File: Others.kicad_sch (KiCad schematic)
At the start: 9 parts, among them J16 UFL, Q14 SI2312BDS

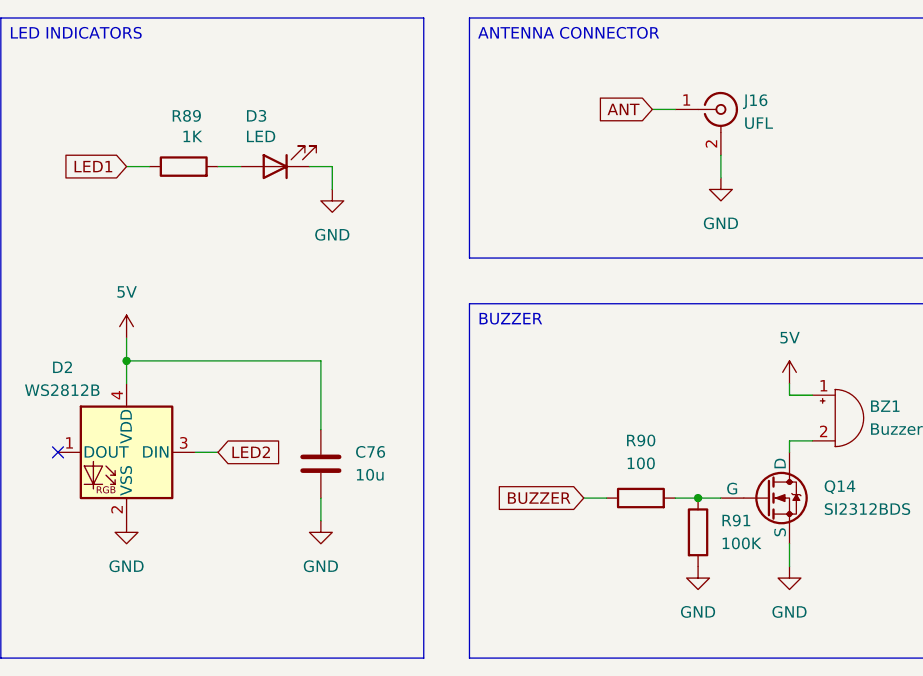
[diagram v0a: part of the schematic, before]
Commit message: Connectors and tag
Added bulk capacitance for each ESC.
Added SWD connector.
Updated all tags.

TODO:
Add pads for the unconnected GPIO pins.
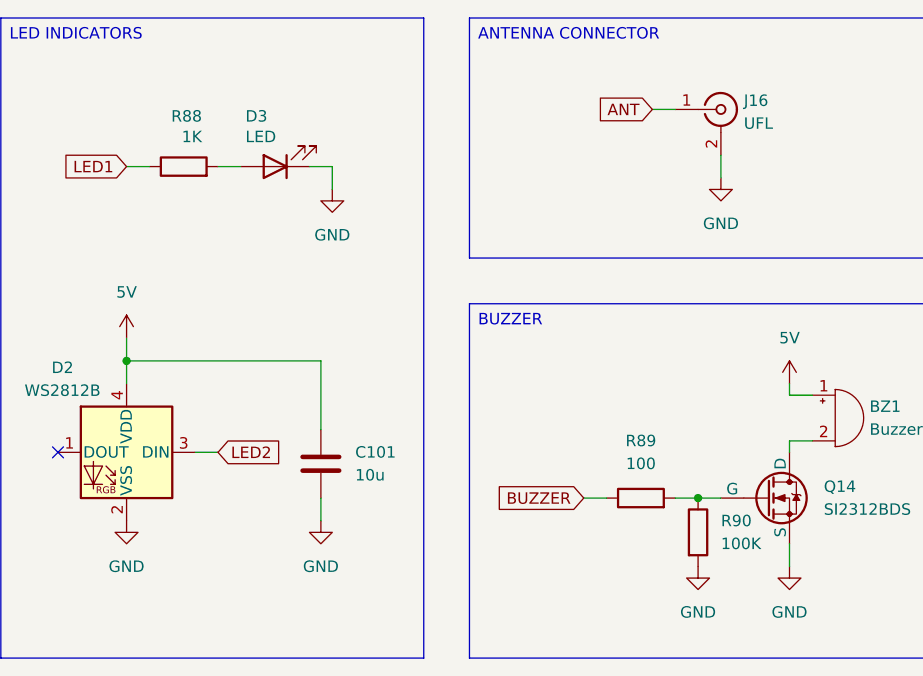
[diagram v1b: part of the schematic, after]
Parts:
- renumbered C76 to C101, R89 to R88, R90 to R89, R91 to R90
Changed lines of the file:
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@@
 		(on_board yes)
 		(dnp no)
-		(property "Reference" "#PWR0186"
+		(property "Reference" "#PWR0198"
 			(at 125.73 85.09 0)
 			(effects
@@
 			(project "ThunderHorse"
 				(path "/ac187c6c-fa53-41cc-bce1-6f39a42a92e8/111cf19a-e0f8-4ba5-b5cb-1102d2b05aed"
-					(reference "#PWR0186")
+					(reference "#PWR0198")
 					(unit 1)
 				)
@@
 		(dnp no)
 		(fields_autoplaced yes)
-		(property "Reference" "#PWR0187"
+		(property "Reference" "#PWR0199"
 			(at 166.37 127 0)
 			(effects
@@
 			(project "ThunderHorse"
 				(path "/ac187c6c-fa53-41cc-bce1-6f39a42a92e8/111cf19a-e0f8-4ba5-b5cb-1102d2b05aed"
-					(reference "#PWR0187")
+					(reference "#PWR0199")
 					(unit 1)
 				)
@@
 		(dnp no)
 		(fields_autoplaced yes)
-		(property "Reference" "#PWR0184"
+		(property "Reference" "#PWR0196"
 			(at 102.87 121.92 0)
 			(effects
@@
 			(project "ThunderHorse"
 				(path "/ac187c6c-fa53-41cc-bce1-6f39a42a92e8/111cf19a-e0f8-4ba5-b5cb-1102d2b05aed"
-					(reference "#PWR0184")
+					(reference "#PWR0196")
 					(unit 1)
 				)
@@
 		(dnp no)
 		(fields_autoplaced yes)
-		(property "Reference" "#PWR0185"
+		(property "Reference" "#PWR0197"
 			(at 124.46 121.92 0)
 			(effects
@@
 			(project "ThunderHorse"
 				(path "/ac187c6c-fa53-41cc-bce1-6f39a42a92e8/111cf19a-e0f8-4ba5-b5cb-1102d2b05aed"
-					(reference "#PWR0185")
+					(reference "#PWR0197")
 					(unit 1)
 				)
@@
 		(dnp no)
 		(fields_autoplaced yes)
-		(property "Reference" "#PWR0188"
+		(property "Reference" "#PWR0200"
 			(at 168.91 83.82 0)
 			(effects
@@
 			(project "ThunderHorse"
 				(path "/ac187c6c-fa53-41cc-bce1-6f39a42a92e8/111cf19a-e0f8-4ba5-b5cb-1102d2b05aed"
-					(reference "#PWR0188")
+					(reference "#PWR0200")
 					(unit 1)
 				)
@@
 		(on_board yes)
 		(dnp no)
-		(property "Reference" "#PWR0189"
+		(property "Reference" "#PWR0201"
 			(at 176.53 104.14 0)
 			(effects
@@
 			(project "ThunderHorse"
 				(path "/ac187c6c-fa53-41cc-bce1-6f39a42a92e8/111cf19a-e0f8-4ba5-b5cb-1102d2b05aed"
-					(reference "#PWR0189")
+					(reference "#PWR0201")
 					(unit 1)
 				)
@@
 		(dnp no)
 		(fields_autoplaced yes)
-		(property "Reference" "R90"
+		(property "Reference" "R89"
 			(at 160.02 106.68 90)
 			(effects
@@
 			(project "ThunderHorse"
 				(path "/ac187c6c-fa53-41cc-bce1-6f39a42a92e8/111cf19a-e0f8-4ba5-b5cb-1102d2b05aed"
-					(reference "R90")
+					(reference "R89")
 					(unit 1)
 				)
@@
 		(on_board yes)
 		(dnp no)
-		(property "Reference" "R89"
+		(property "Reference" "R88"
 			(at 111.252 70.612 90)
 			(effects
@@
 			(project "ThunderHorse"
 				(path "/ac187c6c-fa53-41cc-bce1-6f39a42a92e8/111cf19a-e0f8-4ba5-b5cb-1102d2b05aed"
-					(reference "R89")
+					(reference "R88")
 					(unit 1)
 				)
@@
 		(dnp no)
 		(fields_autoplaced yes)
-		(property "Reference" "R91"
+		(property "Reference" "R90"
 			(at 168.91 115.5699 0)
 			(effects
@@
 			(project "ThunderHorse"
 				(path "/ac187c6c-fa53-41cc-bce1-6f39a42a92e8/111cf19a-e0f8-4ba5-b5cb-1102d2b05aed"
-					(reference "R91")
+					(reference "R90")
 					(unit 1)
 				)
@@
 		(dnp no)
 		(fields_autoplaced yes)
-		(property "Reference" "C76"
+		(property "Reference" "C101"
 			(at 128.27 107.9499 0)
 			(effects
@@
 			(project "ThunderHorse"
 				(path "/ac187c6c-fa53-41cc-bce1-6f39a42a92e8/111cf19a-e0f8-4ba5-b5cb-1102d2b05aed"
-					(reference "C76")
+					(reference "C101")
 					(unit 1)
 				)
@@
 		(dnp no)
 		(fields_autoplaced yes)
-		(property "Reference" "#PWR0190"
+		(property "Reference" "#PWR0202"
 			(at 176.53 127 0)
 			(effects
@@
 			(project "ThunderHorse"
 				(path "/ac187c6c-fa53-41cc-bce1-6f39a42a92e8/111cf19a-e0f8-4ba5-b5cb-1102d2b05aed"
-					(reference "#PWR0190")
+					(reference "#PWR0202")
 					(unit 1)
 				)
@@
 		(on_board yes)
 		(dnp no)
-		(property "Reference" "#PWR0183"
+		(property "Reference" "#PWR0195"
 			(at 102.87 99.06 0)
 			(effects
@@
 			(project "ThunderHorse"
 				(path "/ac187c6c-fa53-41cc-bce1-6f39a42a92e8/111cf19a-e0f8-4ba5-b5cb-1102d2b05aed"
-					(reference "#PWR0183")
-					(unit 1)
-				)
+					(reference "#PWR0195")
+					(unit 1)
+				)

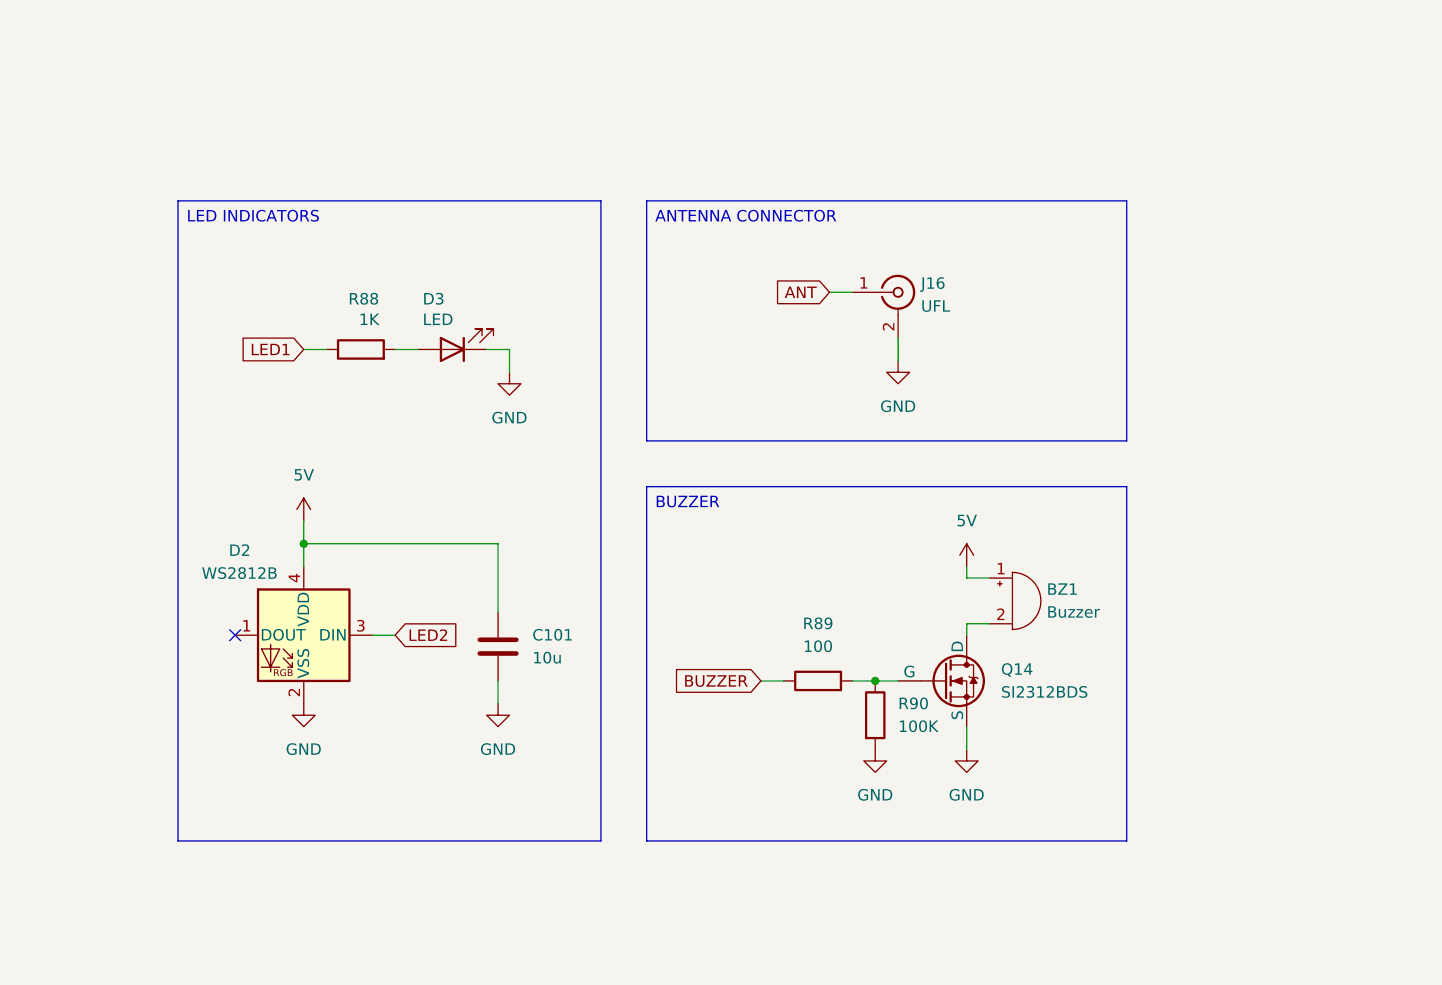
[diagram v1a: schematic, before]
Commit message: Missing labels and revision
First complete revision of the schematic.
Added missing labels.

TODO:
Continue reviewing the schematic.
Include net coloring.
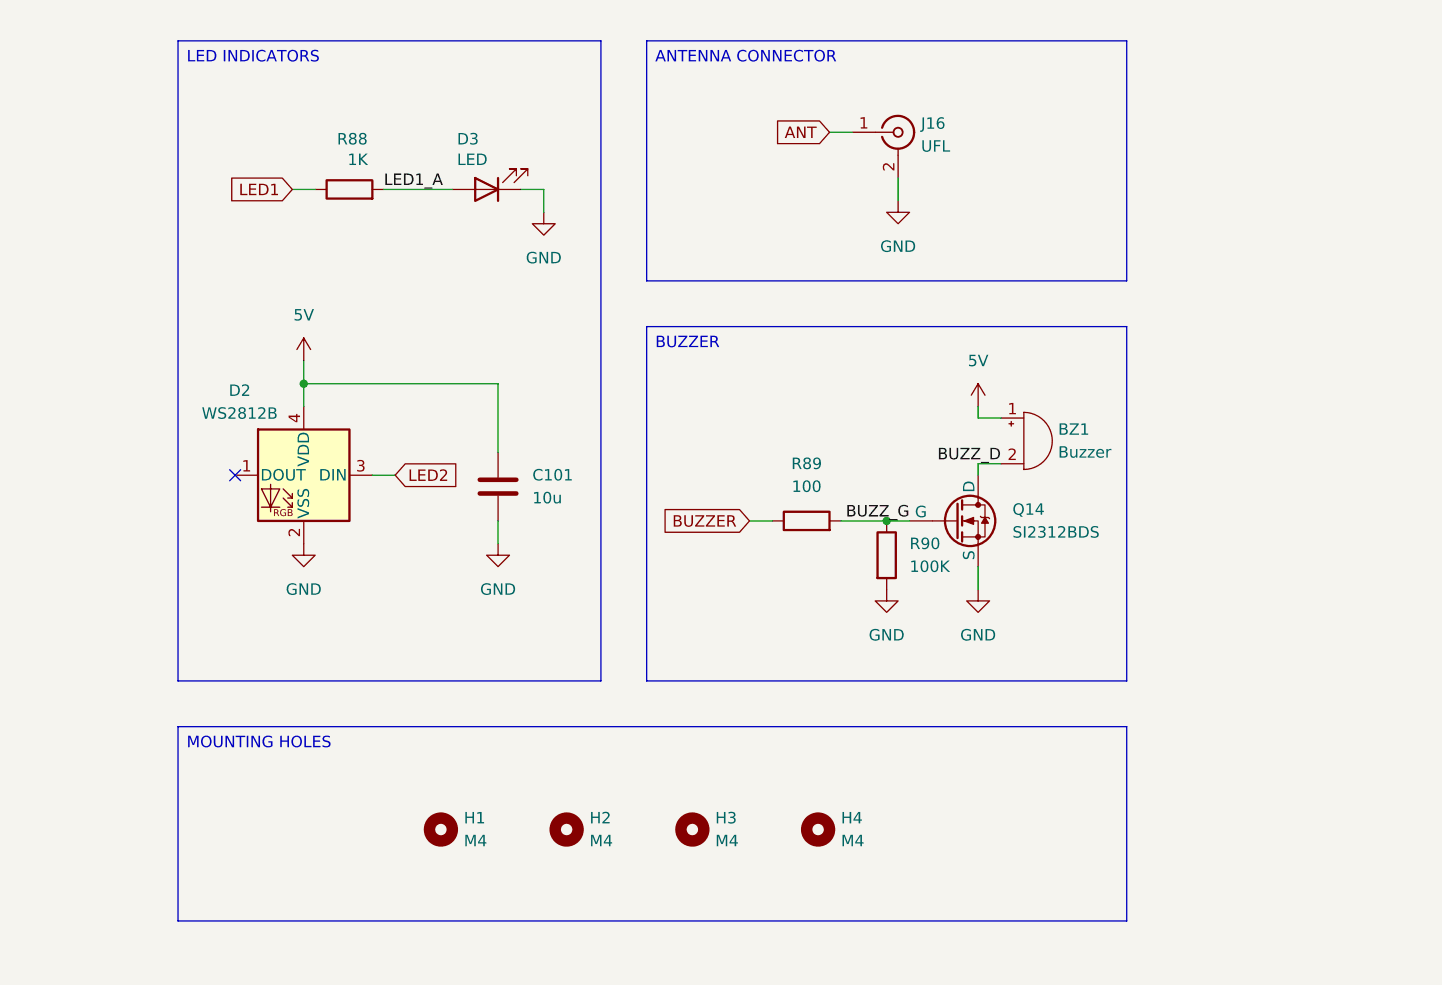
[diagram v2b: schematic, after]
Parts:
- added H1, H2, H3, H4: M4, Custom_Parts:MOUNTING_FC_4.0mm, symbol Mechanical:MountingHole
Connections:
- net LED1_A: now reaches D3.2 (A), R88.2
- net BUZZ_D: now reaches BZ1.2 (-), Q14.3 (D)
- net BUZZ_G: now reaches Q14.1 (G), R89.2, R90.1
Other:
- moved on the sheet: BZ1, C101, D2, D3, J16, Q14, R88, R89, R90

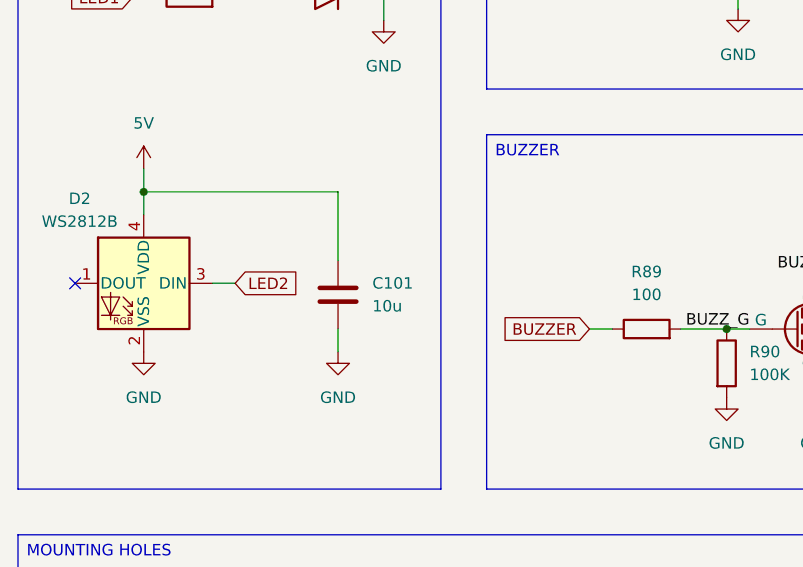
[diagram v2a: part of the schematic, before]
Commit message: ESC layout and footprints
Added the initial ESC layout.
Updated some footprints for compatibility.
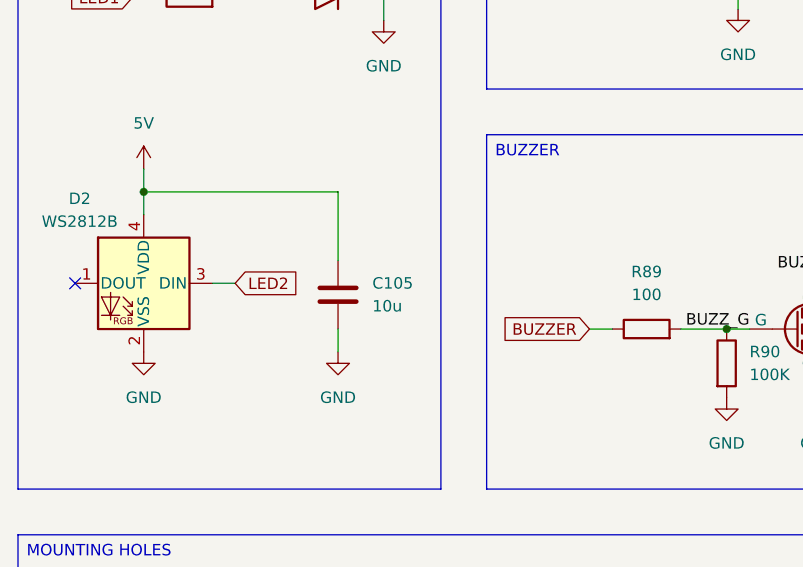
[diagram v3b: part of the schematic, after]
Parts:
- renumbered C101 to C105
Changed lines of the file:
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@@
 		(dnp no)
 		(fields_autoplaced yes)
-		(property "Reference" "C101"
+		(property "Reference" "C105"
 			(at 128.27 90.1699 0)
 			(effects
@@
 			(project "ThunderHorse"
 				(path "/ac187c6c-fa53-41cc-bce1-6f39a42a92e8/111cf19a-e0f8-4ba5-b5cb-1102d2b05aed"
-					(reference "C101")
+					(reference "C105")
 					(unit 1)
 				)

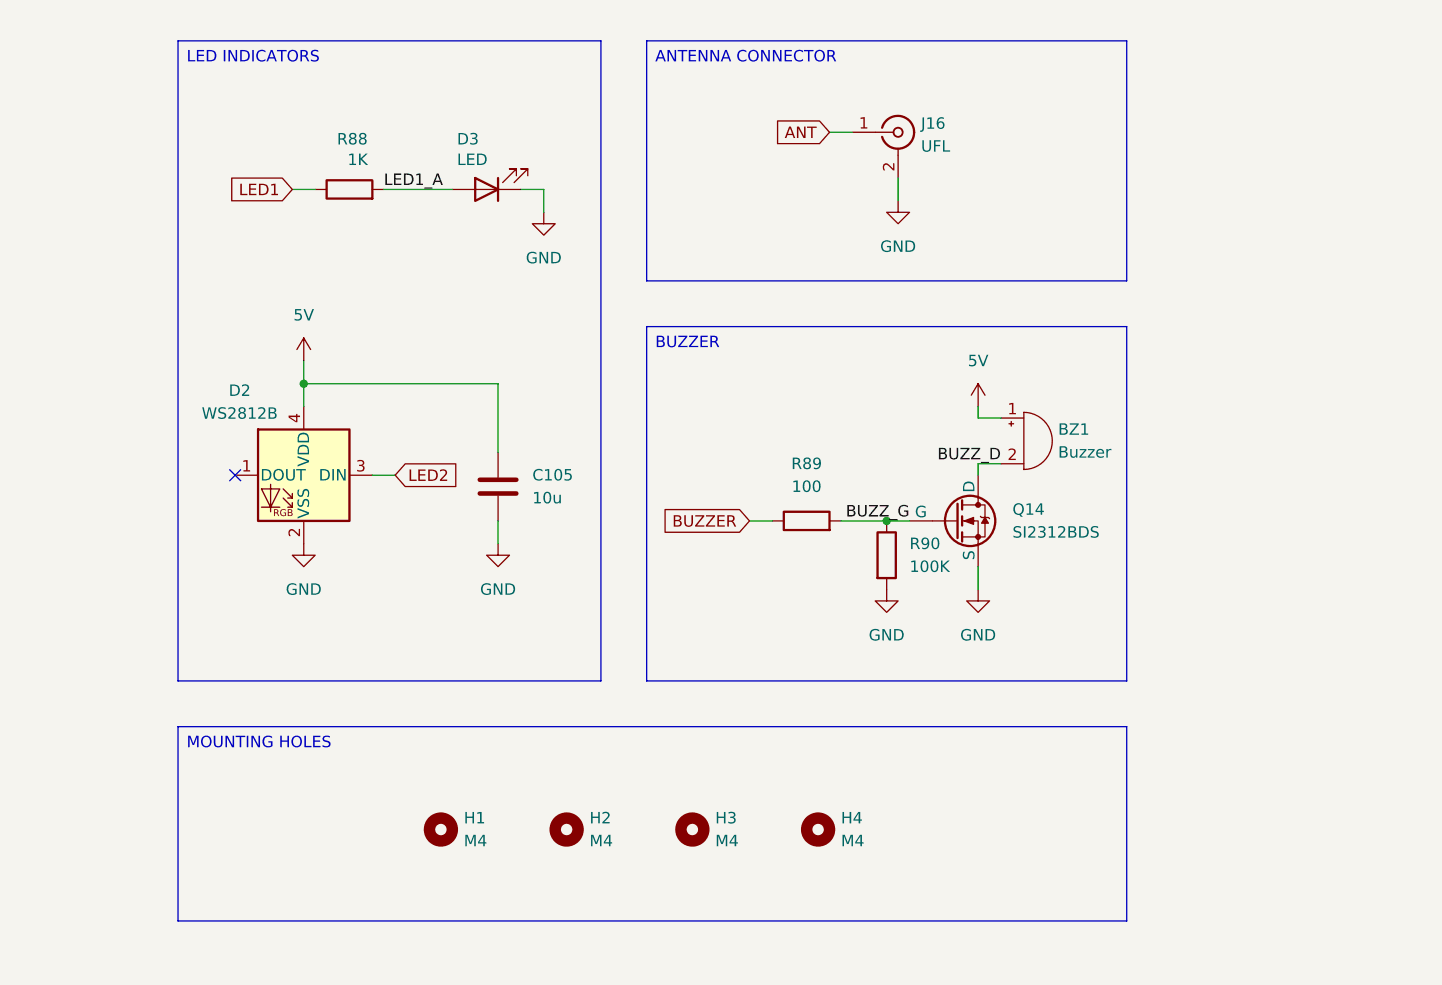
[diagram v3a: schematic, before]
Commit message: Initial layout
Completed an initial layout of the main components.

TODO
Route the ESCs and check the result.
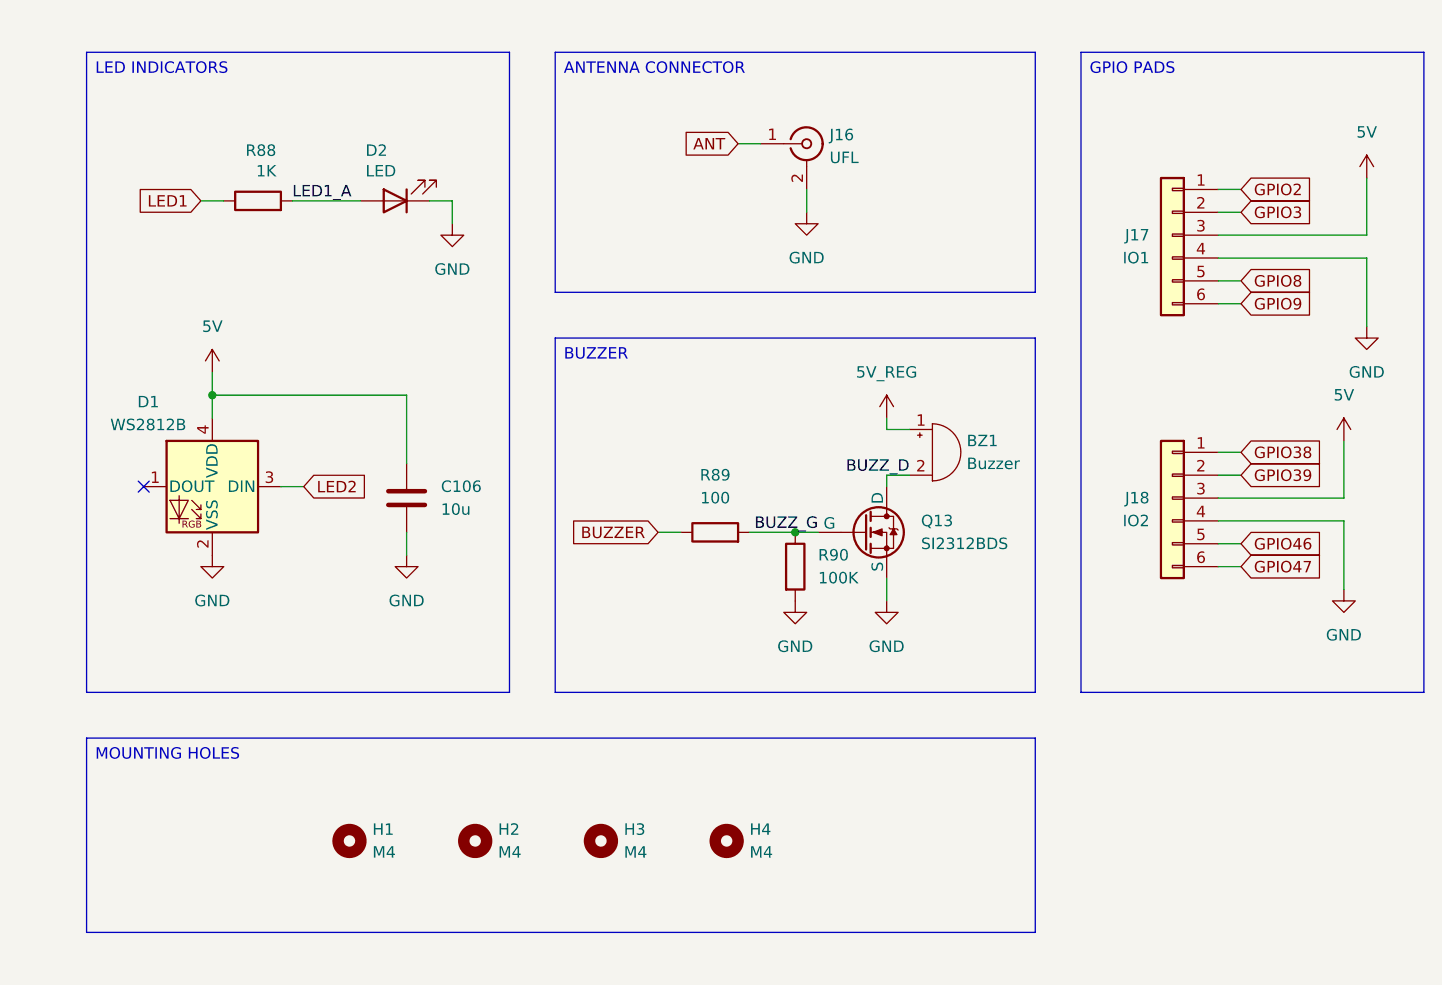
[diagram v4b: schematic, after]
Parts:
- added J17: IO1, Custom_Parts:PAD_6_SQUARE_SOLID_1.5x1.5mm_P2.0mm, symbol Connector_Generic:Conn_01x06
- added J18: IO2, Custom_Parts:PAD_6_SQUARE_SOLID_1.5x1.5mm_P2.0mm, symbol Connector_Generic:Conn_01x06
- renumbered C105 to C106, D2 to D1, D3 to D2, Q14 to Q13
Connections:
- net 5V: now also J17.3 (Pin_3), J18.3 (Pin_3); no longer BZ1.1 (+)
- net GND: now also J17.4 (Pin_4), J18.4 (Pin_4)
- new net 5V_REG: BZ1.1 (+)
- new net GPIO2: J17.1 (Pin_1)
- new net GPIO3: J17.2 (Pin_2)
- new net GPIO38: J18.1 (Pin_1)
- new net GPIO39: J18.2 (Pin_2)
- new net GPIO46: J18.5 (Pin_5)
- new net GPIO47: J18.6 (Pin_6)
- new net GPIO8: J17.5 (Pin_5)
- new net GPIO9: J17.6 (Pin_6)
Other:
- moved on the sheet: BZ1, C106, D1, D2, H1, H2, H3, H4, J16, Q13, R88, R89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
